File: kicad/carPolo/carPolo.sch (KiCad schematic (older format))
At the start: 35 parts, among them Q1 2N3904, Q2 2N3904

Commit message: Finished the Ball & Score Audio section.
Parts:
- added unit 4 of 2B
- added unit 1 of 2B
- added unit 2 of 2B
- added 2C: 7407, symbol 4050
- added C10, C9: 0.1u, symbol C
- added C11: 3.3u, symbol C
- added C12: 100p, symbol C
- added C8: 0.001u, symbol C
- added CR2: DIODE, symbol DIODE
- added I_21: 0, symbol CONN_01X01
- added R10, R22: 100k, symbol R
- added R10: 10000k, symbol R
- added R12, R13, R16, R9: 1000k, symbol R
- added R18: 1500k, symbol R
- added R23, R33: 510k, symbol R
- added R24: 150k, symbol R
- added R31: 22k, symbol R
- added R32: 100k, symbol POT
- added R8: 1.2k, symbol R
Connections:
- net +15V: now also R10.1, R8.1
- net GND: now also C11.2, R32.3
- net VCC: now also 2C.1 (VCC)
- net VSS: now also 2C.8 (VSS)
- net at CR1.2 (K), R5.1, R6.2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: now also 2B.8; no longer 2B.1
- net at R2.1, R4.2: now also 2B.9 (-); no longer 2B.2 (-)
- net at R3.1, R5.2: now also 2B.10 (+); no longer 2B.3 (+)
- net at R30.2: now also R31.2
- new net: C11.1, CR2.1 (A), R13.1, R9.2
- new net: 2B.14, CR2.2 (K), R12.1, R13.2, R16.2, R18.2
- new net: 2C.2, C12.2, R8.2
- new net: 2C.3, I_21.1 (P1)
- new net: 2B.12 (+), R10.1, R12.2
- new net: 2B.13 (-), R10.2, R9.1
- new net: C12.1, R10.2
- new net: 2B.2 (-), C8.2, R16.1
- new net: 2B.1, C8.1, R22.1
- new net: 2B.3 (+), R23.2
- new net: 2B.6 (-), R22.2
- new net: 2B.5 (+), R18.1, R24.2
- new net: 2B.7, R23.1, R24.1, R32.1
- new net: R32.2, R33.2
- new net: C10.2, R33.1
- new net: C9.2, R31.1
- new net: C10.1, C9.1
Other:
- note added: "Bad Schematic Scan - Might not be connected?"
- note added: "Ball + Score Audio"
- note added: "Guess Based on Above"
- note added: "Guess\nBased on\nAbove"
- note added: "Yes, two R10s"

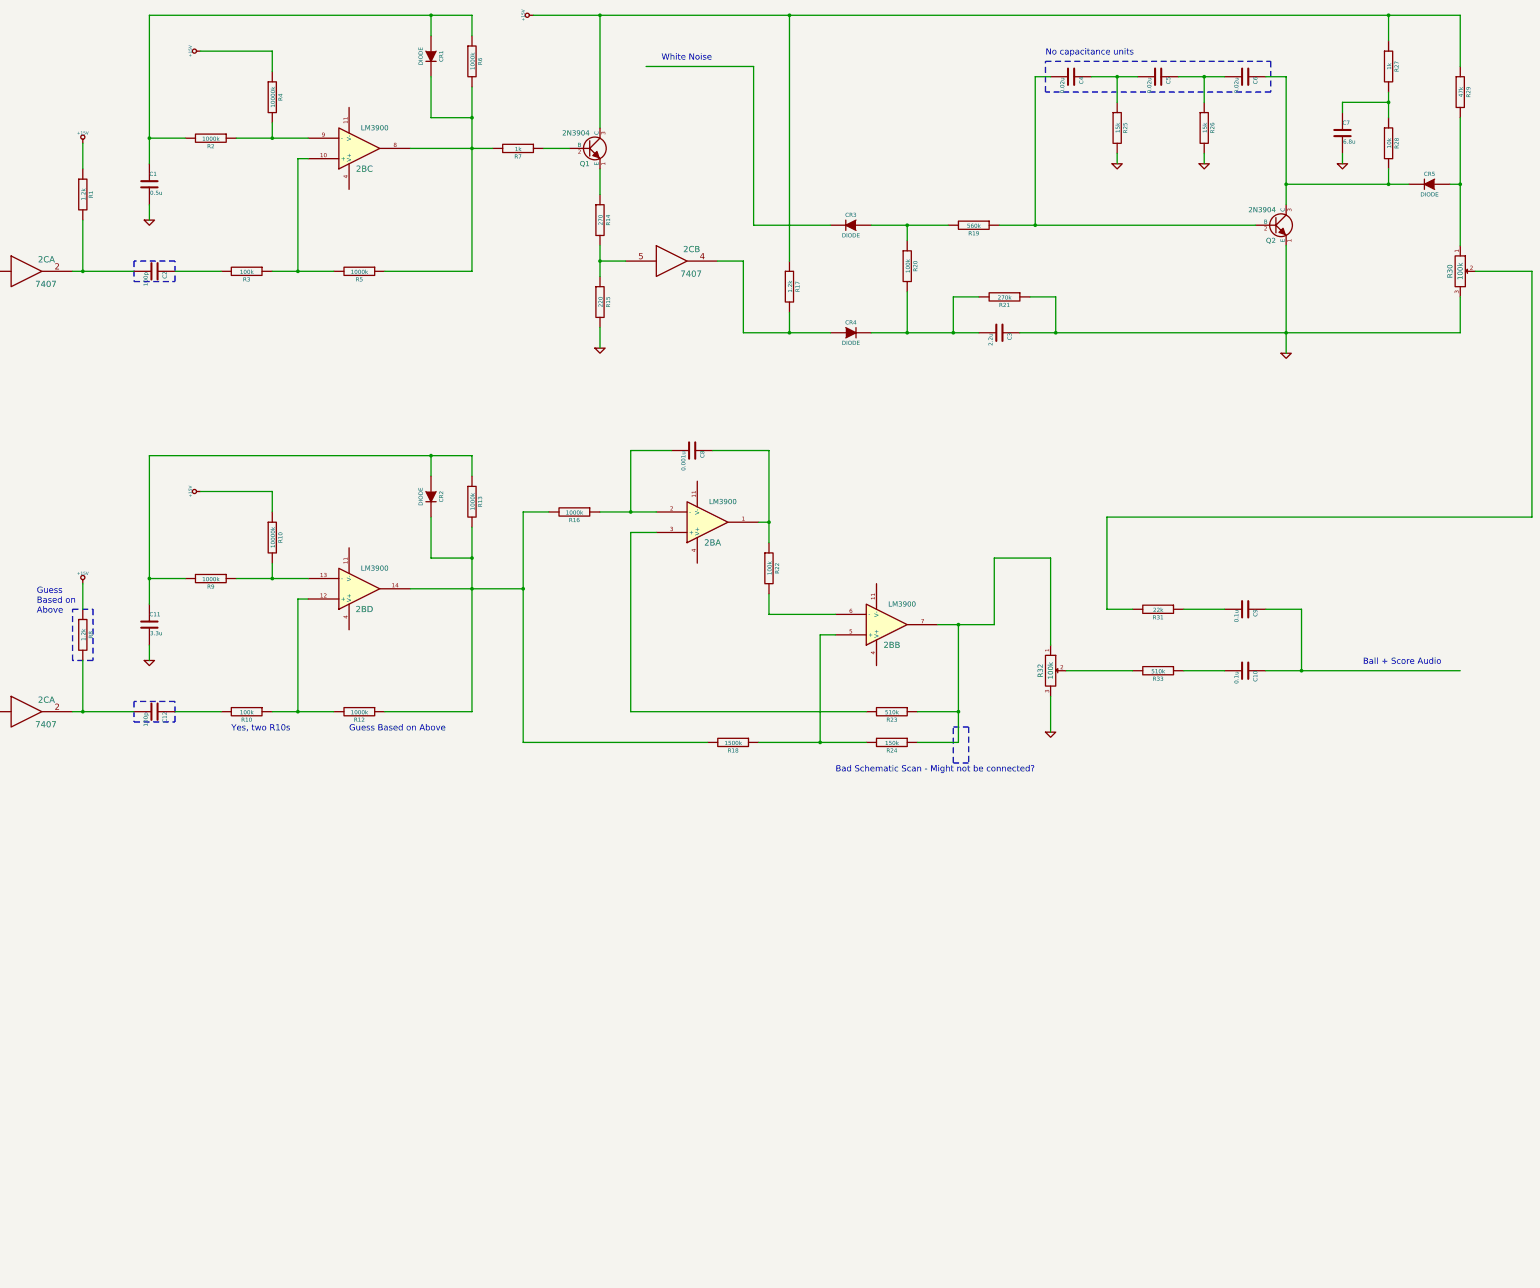
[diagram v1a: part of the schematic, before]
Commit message: Global labels are the way forward.
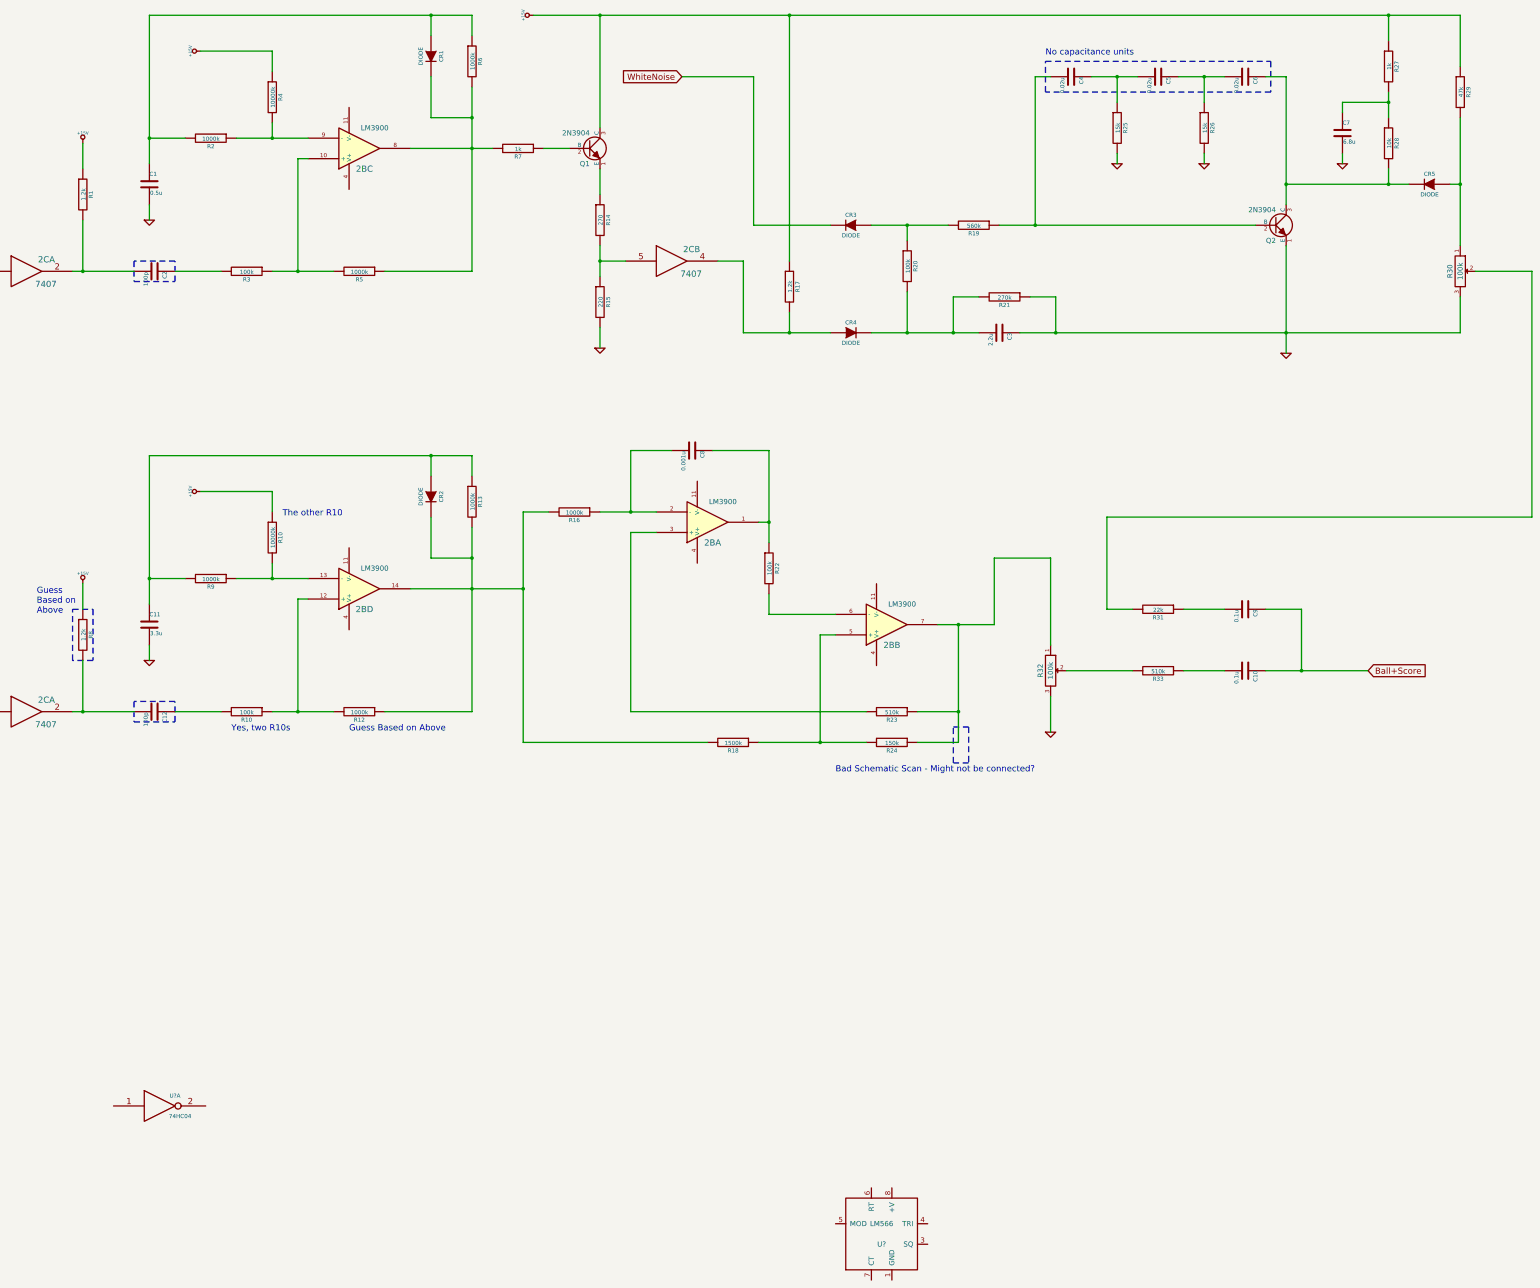
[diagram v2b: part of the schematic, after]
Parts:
- added U?: 74HC04, symbol 74HC04
- added U?: LM566, symbol LM566
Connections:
- net GND: now also U?.7 (GND)
- net VCC: now also U?.14 (VCC)
- net WhiteNoise: now reaches CR3.2 (K)
- net Ball+Score: now reaches C10.1, C9.1
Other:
- note added: "The other R10"
- note removed: "Ball + Score Audio"
- note removed: "White Noise"
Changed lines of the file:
@@
 	1400 3800 1750 3800
 Wire Wire Line
-	2650 3800 3250 3800
+	2650 3800 2750 3800
+Wire Wire Line
+	2750 3800 3250 3800
 Wire Wire Line
 	2750 3300 2750 3800
@@
 	3650 3800 4100 3800
 Wire Wire Line
-	4600 3800 5200 3800
+	4600 3800 4850 3800
+Wire Wire Line
+	4850 3800 5200 3800
 Wire Wire Line
 	4950 2700 4850 2700
@@
 Connection ~ 4850 3800
 Wire Wire Line
-	4250 2500 4950 2500
+	4250 2500 4600 2500
+Wire Wire Line
+	4600 2500 4950 2500
 Wire Wire Line
 	4600 2350 4600 2500
@@
 	3750 2500 3400 2500
 Wire Wire Line
-	3400 1300 3400 2750
+	3400 1300 3400 2500
+Wire Wire Line
+	3400 2500 3400 2750
 Wire Wire Line
 	3400 3150 3400 3300
@@
 	6150 1500 6150 1300
 Wire Wire Line
-	3400 1300 6550 1300
+	3400 1300 6150 1300
+Wire Wire Line
+	6150 1300 6550 1300
 Connection ~ 3400 2500
 Wire Wire Line
@@
 Connection ~ 6150 1300
 Wire Wire Line
-	5950 2600 6750 2600
-Wire Wire Line
-	6550 2000 6550 3800
+	5950 2600 6550 2600
+Wire Wire Line
+	6550 2600 6750 2600
+Wire Wire Line
+	6550 2000 6550 2300
+Wire Wire Line
+	6550 2300 6550 2600
+Wire Wire Line
+	6550 2600 6550 3800
 Wire Wire Line
 	6150 1900 6150 2300
@@
 $EndComp
 Wire Wire Line
-	7150 1300 16200 1300
+	7150 1300 7800 1300
+Wire Wire Line
+	7800 1300 9650 1300
+Wire Wire Line
+	9650 1300 15500 1300
+Wire Wire Line
+	15500 1300 16200 1300
 Wire Wire Line
 	7800 1300 7800 2400
@@
 	7800 2800 7800 3050
 Wire Wire Line
-	7800 3550 7800 3850
+	7800 3550 7800 3700
+Wire Wire Line
+	7800 3700 7800 3850
 Wire Wire Line
 	7800 4350 7800 4550
@@
 	9200 3700 9200 4400
 Wire Wire Line
-	9200 4400 10050 4400
+	9200 4400 9650 4400
+Wire Wire Line
+	9650 4400 10050 4400
 Connection ~ 9650 4400
 Wire Wire Line
@@
 Connection ~ 7800 1300
 Wire Wire Line
-	10450 4400 11500 4400
+	10450 4400 10800 4400
+Wire Wire Line
+	10800 4400 11250 4400
+Wire Wire Line
+	11250 4400 11500 4400
 Wire Wire Line
 	10800 4400 10800 4000
@@
 	10800 3500 10800 3350
 Wire Wire Line
-	10450 3350 11200 3350
+	10450 3350 10800 3350
+Wire Wire Line
+	10800 3350 11200 3350
 Wire Wire Line
 	10050 3350 9300 3350
-Wire Wire Line
-	9300 3350 9300 1800
-Wire Wire Line
-	9300 1800 8250 1800
-Text Notes 8400 1750 0    60   ~ 0
-White Noise
 Connection ~ 10800 4400
 Wire Wire Line
@@
 Connection ~ 11250 4400
 Wire Wire Line
-	11900 4400 16200 4400
+	11900 4400 12250 4400
+Wire Wire Line
+	12250 4400 14500 4400
+Wire Wire Line
+	14500 4400 16200 4400
 Wire Wire Line
 	12000 4050 12250 4050
@@
 $EndComp
 Wire Wire Line
-	12600 1900 13050 1900
-Wire Wire Line
-	13450 1900 13900 1900
+	12600 1900 12850 1900
+Wire Wire Line
+	12850 1900 13050 1900
+Wire Wire Line
+	13450 1900 13700 1900
+Wire Wire Line
+	13700 1900 13900 1900
 Wire Wire Line
 	13700 2150 13700 1900
@@
 $EndComp
 Wire Wire Line
-	11700 3350 14200 3350
-Wire Wire Line
-	14500 3550 14500 4600
+	11700 3350 12050 3350
+Wire Wire Line
+	12050 3350 14200 3350
+Wire Wire Line
+	14500 3550 14500 4400
+Wire Wire Line
+	14500 4400 14500 4600
 Connection ~ 14500 4400
 Wire Wire Line
@@
 	14300 1900 14500 1900
 Wire Wire Line
-	14500 1900 14500 3150
+	14500 1900 14500 2950
+Wire Wire Line
+	14500 2950 14500 3150
 $Comp
 L R R28
@@
 	15500 2800 15500 2950
 Wire Wire Line
-	14500 2950 15700 2950
+	14500 2950 15500 2950
+Wire Wire Line
+	15500 2950 15700 2950
 Connection ~ 14500 2950
 Wire Wire Line
-	15500 2050 15500 2300
+	15500 2050 15500 2150
+Wire Wire Line
+	15500 2150 15500 2300
 Wire Wire Line
 	15500 2150 15050 2150
@@
 	16100 2950 16200 2950
 Wire Wire Line
-	16200 2300 16200 3550
+	16200 2300 16200 2950
+Wire Wire Line
+	16200 2950 16200 3550
 Connection ~ 16200 2950
 Wire Wire Line
@@
 	1400 8100 1750 8100
 Wire Wire Line
-	2650 8100 3250 8100
+	2650 8100 2750 8100
+Wire Wire Line
+	2750 8100 3250 8100
 Wire Wire Line
 	2750 7600 2750 8100
@@
 	3650 8100 4100 8100
 Wire Wire Line
-	4600 8100 5200 8100
+	4600 8100 4850 8100
+Wire Wire Line
+	4850 8100 5200 8100
 Wire Wire Line
 	4950 7000 4850 7000
@@
 Connection ~ 4850 8100
 Wire Wire Line
-	4250 6800 4950 6800
+	4250 6800 4600 6800
+Wire Wire Line
+	4600 6800 4950 6800
 Wire Wire Line
 	4600 6650 4600 6800
@@
 	3750 6800 3400 6800
 Wire Wire Line
-	3400 5600 3400 7050
+	3400 5600 3400 6800
+Wire Wire Line
+	3400 6800 3400 7050
 Wire Wire Line
 	3400 7450 3400 7600
@@
 	6150 5800 6150 5600
 Wire Wire Line
-	3400 5600 6550 5600
+	3400 5600 6150 5600
+Wire Wire Line
+	6150 5600 6550 5600
 Connection ~ 3400 6800
 Wire Wire Line
@@
 Connection ~ 6150 5600
 Wire Wire Line
-	5950 6900 7050 6900
-Wire Wire Line
-	6550 6300 6550 8100
+	5950 6900 6550 6900
+Wire Wire Line
+	6550 6900 7050 6900
+Wire Wire Line
+	6550 6300 6550 6600
+Wire Wire Line
+	6550 6600 6550 6900
+Wire Wire Line
+	6550 6900 6550 8100
 Wire Wire Line
 	6150 6200 6150 6600
@@
 $EndComp
 Wire Wire Line
-	7050 6150 7050 8400
+	7050 6150 7050 6900
+Wire Wire Line
+	7050 6900 7050 8400
 Wire Wire Line
 	7050 6150 7300 6150
@@
 Connection ~ 7050 6900
 Wire Wire Line
-	7800 6150 8350 6150
+	7800 6150 8100 6150
+Wire Wire Line
+	8100 6150 8350 6150
 Wire Wire Line
 	8100 6150 8100 5550
@@
 	9350 6250 9450 6250
 Wire Wire Line
-	9450 5550 9450 6450
+	9450 5550 9450 6250
+Wire Wire Line
+	9450 6250 9450 6450
 Wire Wire Line
 	9450 5550 8900 5550
@@
 	8100 6350 8350 6350
 Wire Wire Line
-	9350 8400 10400 8400
+	9350 8400 9950 8400
+Wire Wire Line
+	9950 8400 10400 8400
 Wire Wire Line
 	10100 7350 9950 7350
@@
 Connection ~ 9950 8400
 Wire Wire Line
-	11100 7250 11650 7250
+	11100 7250 11300 7250
+Wire Wire Line
+	11300 7250 11650 7250
 Wire Wire Line
 	11300 8400 10900 8400
 Wire Wire Line
-	11300 7250 11300 8400
+	11300 7250 11300 8100
+Wire Wire Line
+	11300 8100 11300 8400
 Wire Wire Line
 	10900 8100 11300 8100
@@
 	13500 7700 13900 7700
 Wire Wire Line
-	14300 7700 16200 7700
+	14300 7700 14650 7700
+Wire Wire Line
+	14650 7700 15300 7700
 Wire Wire Line
 	14300 7100 14650 7100
@@
 Wire Wire Line
 	12750 7100 13000 7100
-Text Notes 15250 7650 0    60   ~ 0
-Ball + Score Audio
 Wire Notes Line
 	2650 7100 2850 7100
@@
 Text Notes 5350 8300 0    60   ~ 0
 Guess Based on Above
+Text GLabel 8600 1900 0    60   Input ~ 0
+WhiteNoise
+Wire Wire Line
+	9300 3350 9300 1900
+Wire Wire Line
+	9300 1900 8600 1900
+Text GLabel 15300 7700 2    60   Input ~ 0
+Ball+Score
+Text Notes 4700 6200 0    60   ~ 0
+The other R10
+$Comp
+L 74HC04 U?
+U 1 1 55A94C6F
+P 3500 11950
+F 0 "U?" H 3650 12050 40  0000 C CNN
+F 1 "74HC04" H 3700 11850 40  0000 C CNN
+F 2 "" H 3500 11950 60  0000 C CNN
+F 3 "" H 3500 11950 60  0000 C CNN
+	1    3500 11950
+	1    0    0    -1
+$EndComp
+$Comp
+L LM566 U?
+U 1 1 55A950C2
+P 10550 13200
+F 0 "U?" H 10550 13100 50  0000 C CNN
+F 1 "LM566" H 10550 13300 50  0000 C CNN
+F 2 "" H 10550 13200 50  0001 C CNN
+F 3 "" H 10550 13200 50  0001 C CNN
+	1    10550 13200
+	1    0    0    -1
+$EndComp
 $EndSCHEMATC

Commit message: Some work on car crash #1 audio in Car Polo.
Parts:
- removed 2B: LM3900, symbol LM324
- added 2B, 5K: LM3900, symbol LM3900
- added unit 5 of 6K
- added unit 6 of 6K
- added C18: 0.56u, symbol C
- added I_3, I_B, I_C, I_J: 0, symbol CONN_01X01
- added R60, R61, R62: 1.2k, symbol R
- added R63, R64, R65, R69: 20k, symbol R
- added R66: 680k, symbol R
- added R67, R68, R74: 10k, symbol R
- added R70, R71, R72, R73: 1000k, symbol R
- added R75: 3.3k, symbol R
- added U?: LM380, symbol LM380
- gave numbers to parts that had none: 1
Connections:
- net +15V: now also R60.1, R61.1, R62.1, R71.1, R75.1
- net GND: now also 6K.7 (GND), 6K.7 (GND), R69.2, R74.1, R75.2
- net VCC: now also 6K.14 (VCC), 6K.14 (VCC)
- net at CR1.2 (K), R5.1, R6.2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: now also 2B.9
- net at R3.1, R5.2: now also 2B.13 (+)
- net at R2.1, R4.2: now also 2B.8 (-)
- net at CR2.2 (K), R12.1, R13.2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: now also 2B.10
- net at R10.1, R12.2: now also 2B.12 (+)
- net at R10.2, R9.1: now also 2B.11 (-)
- net at C8.2, R16.1: now also 2B.3 (-)
- net at C8.1, R22.1: now also 2B.4
- net at R23.2: now also 2B.2 (+)
- net at R22.2: now also 2B.6 (-)
- net at R18.1, R24.2: now also 2B.1 (+)
- net at R23.1, R24.1, R32.1: now also 2B.5
- new net: 6K.8, R60.2, R63.2
- new net: 6K.9, I_C.1 (P1)
- new net: 6K.10, R61.2, R64.2
- new net: 6K.11, I_B.1 (P1)
- new net: 6K.12, R62.2, R65.2
- new net: 6K.13, I_3.1 (P1)
- new net: R63.1, R66.2, R67.1
- new net: R64.1, R67.2, R68.1
- new net: R65.1, R68.2, R69.1
- new net: 5K.13 (+), R66.1
- new net: 5K.8 (-), C18.2, R70.2
- new net: 5K.9, C18.1, R70.1, R72.2
- new net: 5K.11 (-), R72.1, R73.2
- new net: 5K.10, R73.1, R74.2
- new net: 5K.12 (+), R71.2
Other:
- note added: "PLR 1\nSPEED\n 0"
- note added: "PLR 1\nSPEED\n 1"
- note added: "PLR 1\nSPEED\n 2"
- moved on the sheet: U?
